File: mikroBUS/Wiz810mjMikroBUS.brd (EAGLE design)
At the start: 63.5 x 38.4 mm, 3 parts

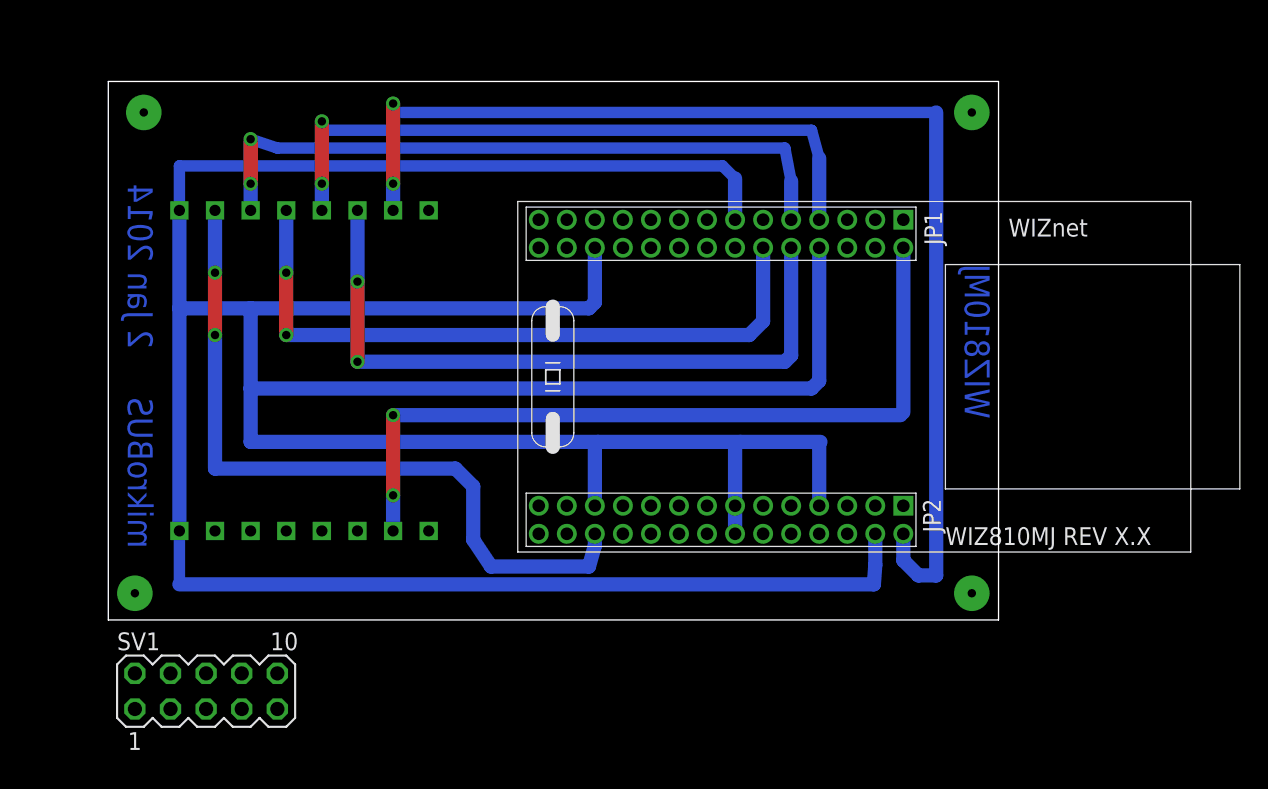
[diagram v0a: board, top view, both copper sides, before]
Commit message: 
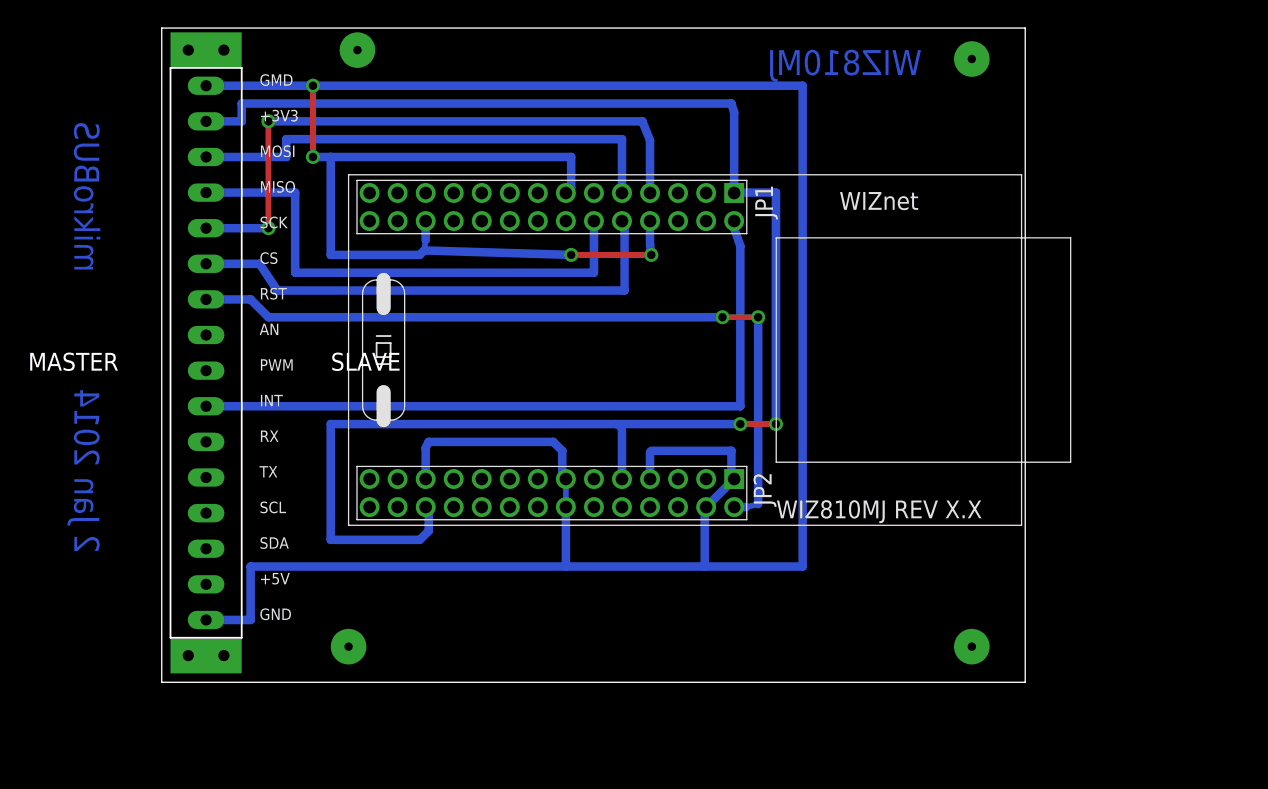
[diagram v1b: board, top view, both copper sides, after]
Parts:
- removed SV1: (no value), con-lstb:MA05-2
- U$2: device lieven:MIKROBUS -> lieven:MIKROBUS_SIL
- moved U$1 12.2 mm to (17.1, 31.8)
- moved U$2 9.09 mm to (6.99, 20.3), turned to 0 degrees
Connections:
- net N$3 renamed GND
- removed net N$9: U$1.52, U$2.+3.3V
- new net +3V3: U$1.1, U$1.37, U$1.52, U$2.+3.3V
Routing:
- net +3V3: track 0.00 -> 117.8 mm, vias 0 -> 2
- net GND: track 276.0 -> 221.8 mm, vias 0 -> 4
- net N$9: track 52.8 -> 0.00 mm, vias 2 -> 0
- net N$4: track 84.3 -> 55.0 mm
- net N$5: track 49.6 -> 35.8 mm, vias 2 -> 0
- net N$7: track 48.4 -> 34.8 mm, vias 2 -> 0
- net N$6: track 48.5 -> 37.1 mm, vias 2 -> 0
- net N$1: track 56.5 -> 51.4 mm, vias 2 -> 0
- net N$3: track 48.4 -> 44.0 mm
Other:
- board size 63.5 x 38.4 mm -> 61.6 x 46.7 mm
